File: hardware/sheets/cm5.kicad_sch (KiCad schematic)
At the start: 28 parts, among them J3 microSD, J4 RJ45 GbE magjack UDE RB1-125B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, J40 Fan GND/5V/TACH/PWM, J41 OLED GND/VCC/SCL/SDA, J5 USB-C rpiboot, J6 nRPIBOOT, J7 UART0 GND/TX/RX, M1 CM5002016 (J1), M2 CM5002016 (J2), Q1 2N7002, SW1 DIP x8

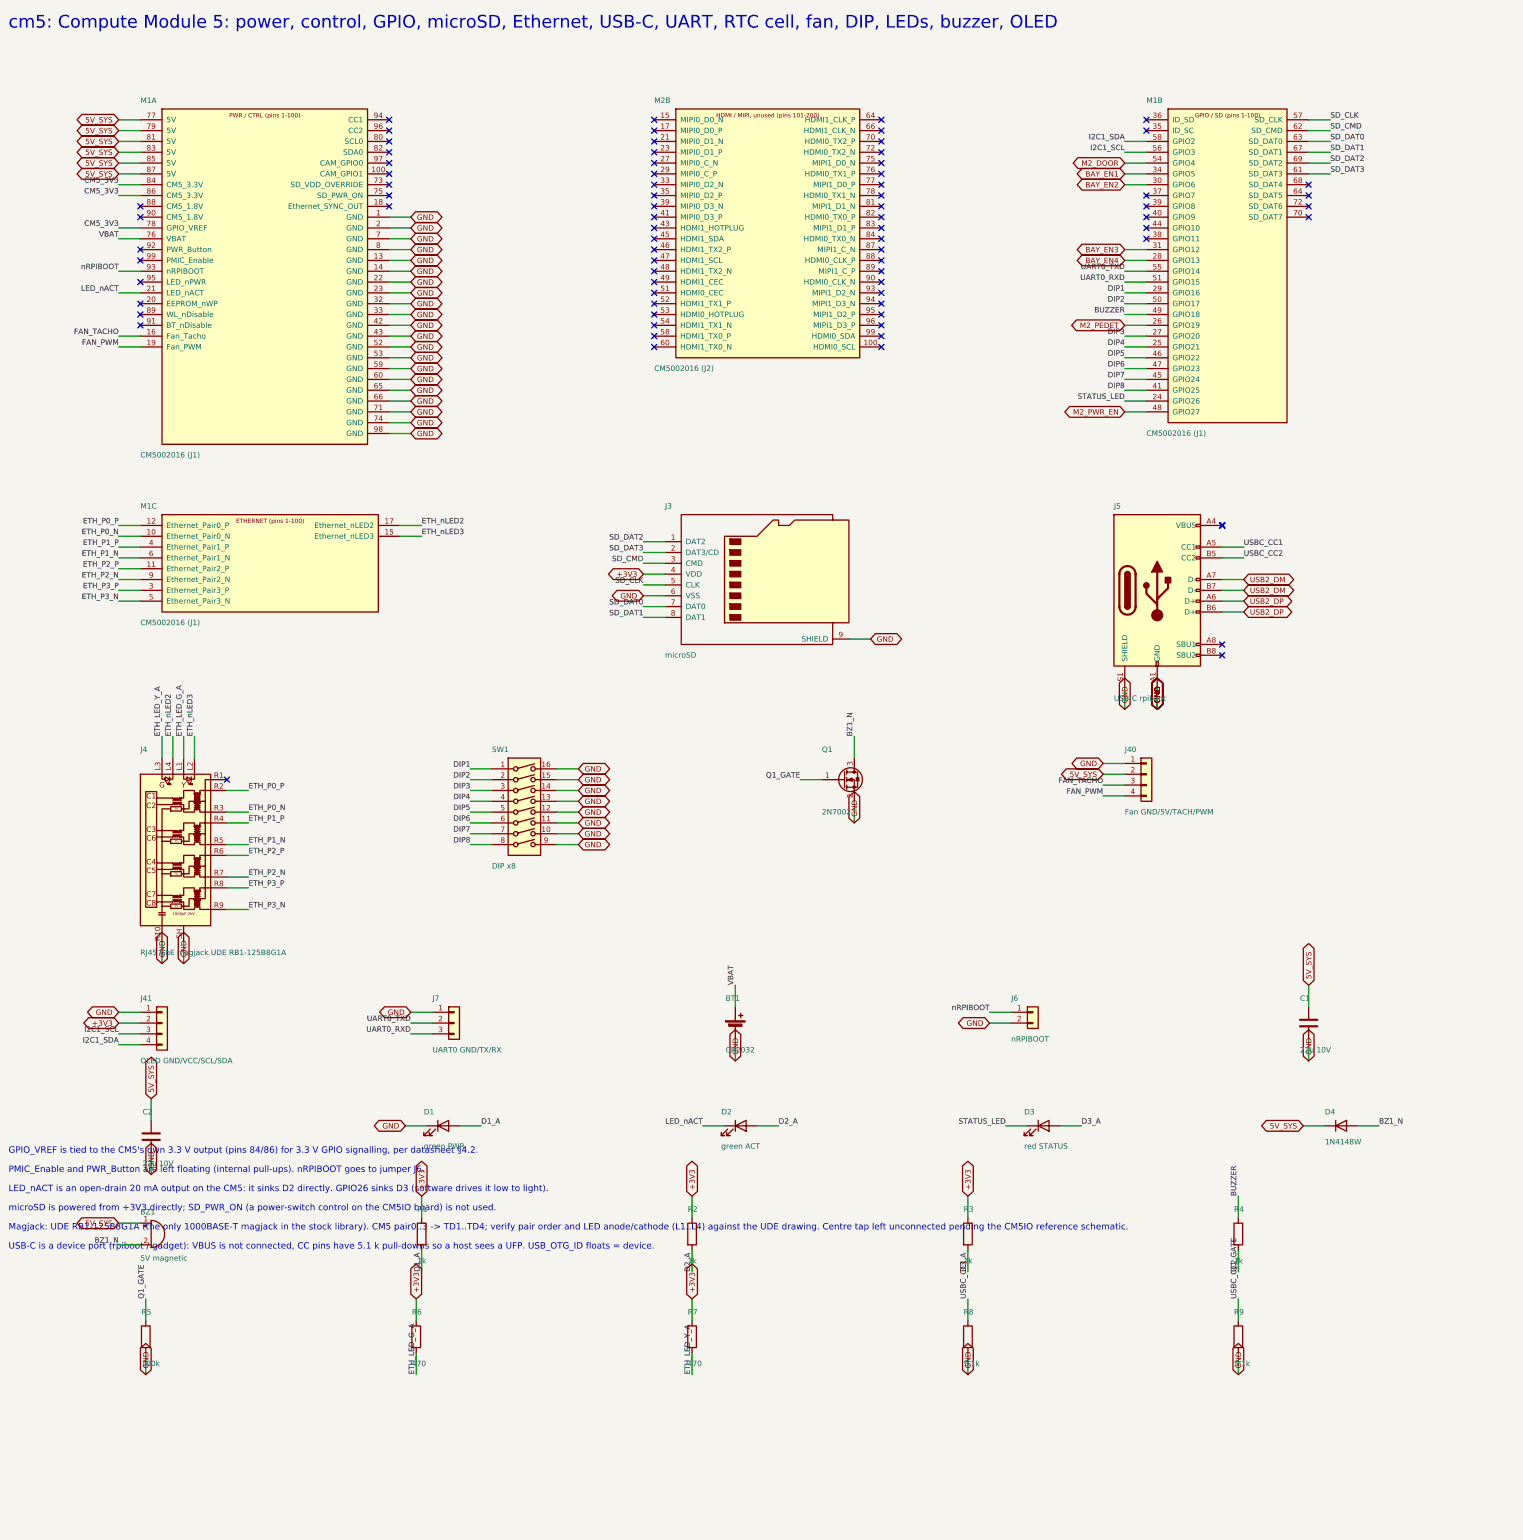
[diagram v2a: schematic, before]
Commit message: hardware: CM5 on the official 204-pad footprint, CM5IO M.2 footprint, reference-design fixes
From the Raspberry Pi CM5IO rev 2 KiCad files: single CM5 footprint with both
connectors and mounting holes; M.2 socket footprint; USB-C CC pins to the CM5;
fan PWM pull-up; microSD through a load switch on SD_PWR_ON; M.2 shield and
standoff pads to GND; PCIe polarity note. Board regenerated with the module
and M.2 at their real sizes; centre mounting hole dropped.

Co-Authored-By: Claude Fable 5.1 <noreply@anthropic.com>
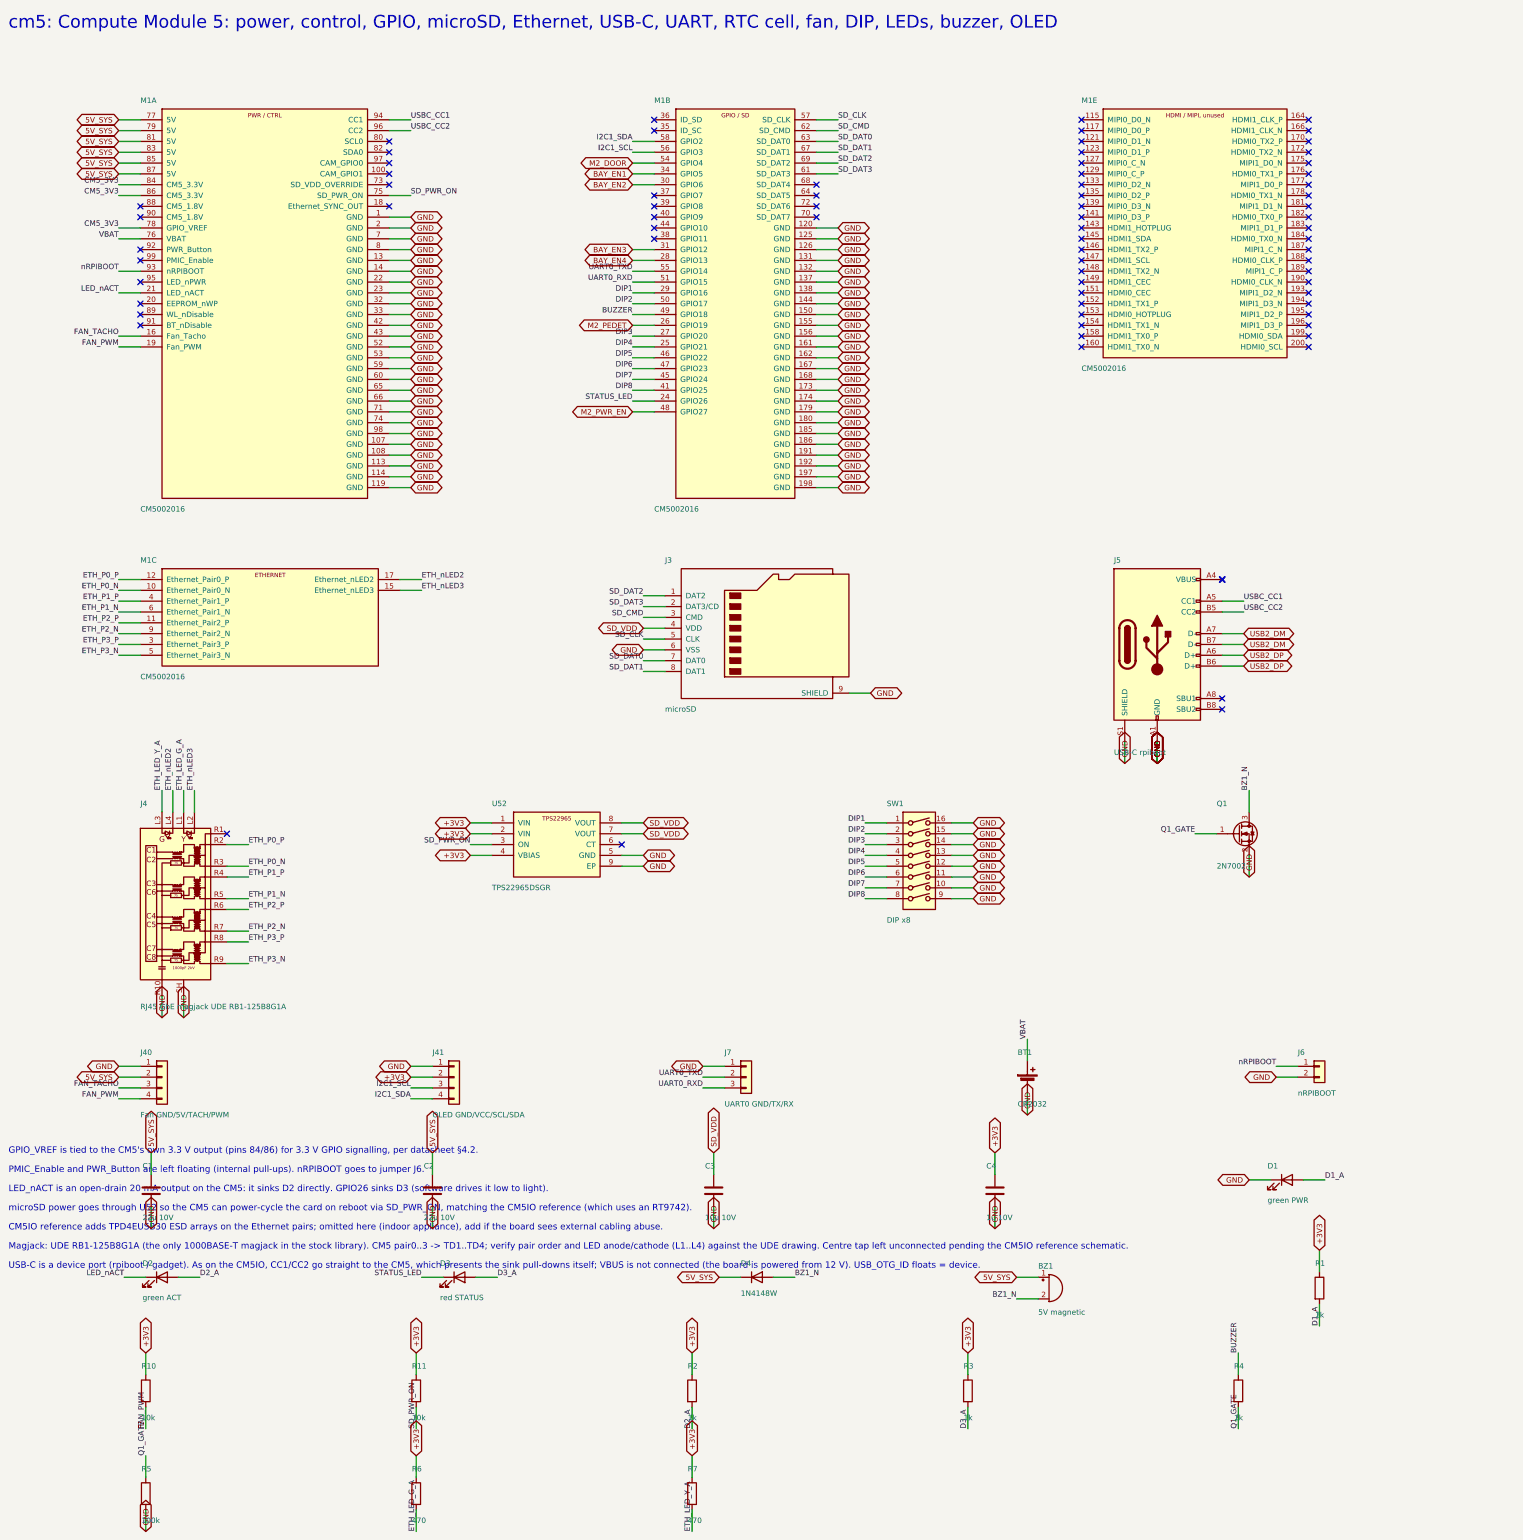
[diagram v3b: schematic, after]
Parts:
- added R5: 100k, Resistor_SMD:R_0402_1005Metric, symbol Device:R
- added R6, R7: 470, Resistor_SMD:R_0402_1005Metric, symbol Device:R
- BT1: renamed from J6; value nRPIBOOT -> CR2032; footprint Connector_PinHeader_2.54mm:PinHeader_1x02_P2.54mm_Vertical -> Battery:BatteryHolder_Keystone_1060_1x2032; symbol Connector_Generic:Conn_01x02 -> Device:Battery_Cell
- BZ1: renamed from R3; value 1k -> 5V magnetic; footprint Resistor_SMD:R_0603_1608Metric -> Buzzer_Beeper:Buzzer_12x9.5RM7.6; symbol Device:R -> Device:Buzzer
- C2: renamed from D1; value green PWR -> 22u 10V; footprint LED_THT:LED_D3.0mm -> Capacitor_SMD:C_0805_2012Metric; symbol Device:LED -> Device:C
- C3: renamed from D2; value green ACT -> 10u 10V; footprint LED_THT:LED_D3.0mm -> Capacitor_SMD:C_0805_2012Metric; symbol Device:LED -> Device:C
- C4: renamed from D3; value red STATUS -> 1u 10V; footprint LED_THT:LED_D3.0mm -> Capacitor_SMD:C_0402_1005Metric; symbol Device:LED -> Device:C
- D1: renamed from D4; value 1N4148W -> green PWR; footprint Diode_SMD:D_SOD-123 -> LED_THT:LED_D3.0mm; symbol Device:D -> Device:LED
- D2: renamed from BZ1; value 5V magnetic -> green ACT; footprint Buzzer_Beeper:Buzzer_12x9.5RM7.6 -> LED_THT:LED_D3.0mm; symbol Device:Buzzer -> Device:LED
- D3: renamed from R1; value 1k -> red STATUS; footprint Resistor_SMD:R_0603_1608Metric -> LED_THT:LED_D3.0mm; symbol Device:R -> Device:LED
- D4: renamed from R2; value 1k -> 1N4148W; footprint Resistor_SMD:R_0603_1608Metric -> Diode_SMD:D_SOD-123; symbol Device:R -> Device:D
- J40: renamed from J41; value OLED GND/VCC/SCL/SDA -> Fan GND/5V/TACH/PWM; footprint Connector_PinHeader_2.54mm:PinHeader_1x04_P2.54mm_Vertical -> Connector:FanPinHeader_1x04_P2.54mm_Vertical
- J41: renamed from J7; value UART0 GND/TX/RX -> OLED GND/VCC/SCL/SDA; footprint Connector_PinHeader_2.54mm:PinHeader_1x03_P2.54mm_Vertical -> Connector_PinHeader_2.54mm:PinHeader_1x04_P2.54mm_Vertical; symbol Connector_Generic:Conn_01x03 -> Connector_Generic:Conn_01x04
- J6: renamed from C1; value 22u 10V -> nRPIBOOT; footprint Capacitor_SMD:C_0805_2012Metric -> Connector_PinHeader_2.54mm:PinHeader_1x02_P2.54mm_Vertical; symbol Device:C -> Connector_Generic:Conn_01x02
- J7: renamed from BT1; value CR2032 -> UART0 GND/TX/RX; footprint Battery:BatteryHolder_Keystone_1060_1x2032 -> Connector_PinHeader_2.54mm:PinHeader_1x03_P2.54mm_Vertical; symbol Device:Battery_Cell -> Connector_Generic:Conn_01x03
- M1: value CM5002016 (J1) -> CM5002016; footprint Connector_Hirose_DF40:Hirose_DF40C-100DS-0.4V_2x50_P0.4mm -> brain-drain:Raspberry-Pi-5-Compute-Module; symbol brain-drain:CM5_J1 -> brain-drain:CM5
- M1: renamed from M2; value CM5002016 (J2) -> CM5002016; footprint Connector_Hirose_DF40:Hirose_DF40C-100DS-0.4V_2x50_P0.4mm -> brain-drain:Raspberry-Pi-5-Compute-Module; symbol brain-drain:CM5_J2 -> brain-drain:CM5
- Q1: renamed from J40; value Fan GND/5V/TACH/PWM -> 2N7002; footprint Connector:FanPinHeader_1x04_P2.54mm_Vertical -> Package_TO_SOT_SMD:SOT-23; symbol Connector_Generic:Conn_01x04 -> Transistor_FET:2N7002
- R1: renamed from R4; footprint Resistor_SMD:R_0402_1005Metric -> Resistor_SMD:R_0603_1608Metric
- R10: renamed from R5; value 100k -> 10k
- R11: renamed from R6; value 470 -> 10k
- R2: renamed from R7; value 470 -> 1k; footprint Resistor_SMD:R_0402_1005Metric -> Resistor_SMD:R_0603_1608Metric
- R3: renamed from R8; value 5.1k -> 1k; footprint Resistor_SMD:R_0402_1005Metric -> Resistor_SMD:R_0603_1608Metric
- R4: renamed from R9; value 5.1k -> 1k
- SW1: renamed from Q1; value 2N7002 -> DIP x8; footprint Package_TO_SOT_SMD:SOT-23 -> Button_Switch_THT:SW_DIP_SPSTx08_Piano_10.8x21.88mm_W7.62mm_P2.54mm; symbol Transistor_FET:2N7002 -> Switch:SW_DIP_x08
- U52: renamed from SW1; value DIP x8 -> TPS22965DSGR; footprint Button_Switch_THT:SW_DIP_SPSTx08_Piano_10.8x21.88mm_W7.62mm_P2.54mm -> Package_SON:Texas_DSG0008A_WSON-8-1EP_2x2mm_P0.5mm_EP0.9x1.6mm; symbol Switch:SW_DIP_x08 -> brain-drain:TPS22965
- renumbered C2 to C1
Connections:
- net +3V3: now also C4.1, J41.2 (Pin_2), R1.1, R10.1, R3.1, U52.1 (VIN), U52.2 (VIN), U52.4 (VBIAS), R6.1, R7.1; no longer BZ1.1, D3.1, D4.1, J3.4 (VDD), J40.2 (Pin_2)
- net 5V_SYS: now also BZ1.1 (+), C2.1, D4.1 (K), J40.2 (Pin_2); no longer D1.1 (K), D2.1 (+), J6.1, Q1.2 (Pin_2)
- net BAY_EN1: now also M1.34 (GPIO5); no longer M1.34 (GPIO5)
- net BAY_EN2: now also M1.30 (GPIO6); no longer M1.30 (GPIO6)
- net BAY_EN3: now also M1.31 (GPIO12); no longer M1.31 (GPIO12)
- net BAY_EN4: now also M1.28 (GPIO13); no longer M1.28 (GPIO13)
- net BUZZER: now also M1.49 (GPIO18), R4.1; no longer M1.49 (GPIO18), R1.1
- net BZ1_N: now also BZ1.2 (-), D4.2 (A), Q1.3 (D); no longer D1.2 (A), D2.2 (-), SW1.3 (D)
- net D1_A: now also D1.2 (A), R1.2; no longer C2.2 (A), D3.2
- net D2_A: now also D2.2 (A), R2.2; no longer C3.2 (A), D4.2
- net D3_A: now also D3.2 (A), R3.2; no longer BZ1.2, C4.2 (A)
- net DIP1: now also M1.29 (GPIO16), SW1.1; no longer M1.29 (GPIO16), U52.1
- net DIP2: now also M1.50 (GPIO17), SW1.2; no longer M1.50 (GPIO17), U52.2
- net DIP3: now also M1.27 (GPIO20), SW1.3; no longer M1.27 (GPIO20), U52.3
- net DIP4: now also M1.25 (GPIO21), SW1.4; no longer M1.25 (GPIO21), U52.4
- net DIP5: now also M1.46 (GPIO22), SW1.5; no longer M1.46 (GPIO22), U52.5
- net DIP6: now also M1.47 (GPIO23), SW1.6; no longer M1.47 (GPIO23), U52.6
- net DIP7: now also M1.45 (GPIO24), SW1.7; no longer M1.45 (GPIO24), U52.7
- net DIP8: now also M1.41 (GPIO25), SW1.8; no longer M1.41 (GPIO25), U52.8
- net ETH_LED_G_A: now also R6.2; no longer R11.2
- net ETH_LED_Y_A: now also R7.2; no longer R2.2
- net FAN_PWM: now also J40.4 (Pin_4), R10.2; no longer Q1.4 (Pin_4)
- net FAN_TACHO: now also J40.3 (Pin_3); no longer Q1.3 (Pin_3)
- net GND: now also C2.2, C3.2, C4.2, D1.1 (K), J7.1 (Pin_1), M1.107 (GND), M1.108 (GND), M1.113 (GND), M1.114 (GND), M1.119 (GND), M1.120 (GND), M1.125 (GND), M1.126 (GND), M1.131 (GND), M1.132 (GND), M1.137 (GND), M1.138 (GND), M1.144 (GND), M1.150 (GND), M1.155 (GND), M1.156 (GND), M1.161 (GND), M1.162 (GND), M1.167 (GND), M1.168 (GND), M1.173 (GND), M1.174 (GND), M1.179 (GND), M1.180 (GND), M1.185 (GND), M1.186 (GND), M1.191 (GND), M1.192 (GND), M1.197 (GND), M1.198 (GND), Q1.2 (S), SW1.10, SW1.11, SW1.12, SW1.13, SW1.14, SW1.15, SW1.16, SW1.9, U52.5 (GND), R5.2; no longer C2.1 (K), J7.2 (-), Q1.1 (Pin_1), R10.2, R3.2, R4.2, SW1.2 (S), U52.10, U52.11, U52.12, U52.13, U52.14, U52.15, U52.16
- net I2C1_SCL: now also J41.3 (Pin_3), M1.56 (GPIO3); no longer J40.3 (Pin_3), M1.56 (GPIO3)
- net I2C1_SDA: now also J41.4 (Pin_4), M1.58 (GPIO2); no longer J40.4 (Pin_4), M1.58 (GPIO2)
- net LED_nACT: now also D2.1 (K); no longer C3.1 (K)
- net M2_DOOR: now also M1.54 (GPIO4); no longer M1.54 (GPIO4)
- net M2_PEDET: now also M1.26 (GPIO19); no longer M1.26 (GPIO19)
- net M2_PWR_EN: now also M1.48 (GPIO27); no longer M1.48 (GPIO27)
- net Q1_GATE: now also Q1.1 (G), R4.2, R5.1; no longer R1.2, R10.1, SW1.1 (G)
- net SD_CLK: now also M1.57 (SD_CLK); no longer M1.57 (SD_CLK)
- net SD_CMD: now also M1.62 (SD_CMD); no longer M1.62 (SD_CMD)
- net SD_DAT0: now also M1.63 (SD_DAT0); no longer M1.63 (SD_DAT0)
- net SD_DAT1: now also M1.67 (SD_DAT1); no longer M1.67 (SD_DAT1)
- net SD_DAT2: now also M1.69 (SD_DAT2); no longer M1.69 (SD_DAT2)
- net SD_DAT3: now also M1.61 (SD_DAT3); no longer M1.61 (SD_DAT3)
- net STATUS_LED: now also D3.1 (K), M1.24 (GPIO26); no longer C4.1 (K), M1.24 (GPIO26)
- net UART0_RXD: now also J7.3 (Pin_3), M1.51 (GPIO15); no longer J41.3 (Pin_3), M1.51 (GPIO15)
- net UART0_TXD: now also J7.2 (Pin_2), M1.55 (GPIO14); no longer J41.2 (Pin_2), M1.55 (GPIO14)
- net USBC_CC1: now also M1.94 (CC1); no longer R3.1
- net USBC_CC2: now also M1.96 (CC2); no longer R4.1
- net VBAT: now also BT1.1 (+); no longer J7.1 (+)
- net nRPIBOOT: now also J6.1 (Pin_1); no longer BT1.1 (Pin_1)
- net SD_PWR_ON: now reaches M1.75 (SD_PWR_ON)
- net SD_PWR_ON: now also R11.2, U52.3 (ON)
- new net SD_VDD: C3.1, J3.4 (VDD), U52.7 (VOUT), U52.8 (VOUT)
- no-connect marks 79 -> 77
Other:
- note added: "CM5IO reference adds TPD4EUSB30 ESD arrays on the Ethernet pairs; omitted here (indoor appliance), add if the board sees external cabling abuse."
- note added: "USB-C is a device port (rpiboot / gadget). As on the CM5IO, CC1/CC2 go straight to the CM5, which presents the sink pull-downs itself; VBUS is not connected (the board is powered from 12 V). USB_OTG_ID floats = device."
- note added: "microSD power goes through U52 so the CM5 can power-cycle the card on reboot via SD_PWR_ON, matching the CM5IO reference (which uses an RT9742)."
- note removed: "USB-C is a device port (rpiboot / gadget): VBUS is not connected, CC pins have 5.1 k pull-downs so a host sees a UFP. USB_OTG_ID floats = device."
- note removed: "microSD is powered from +3V3 directly; SD_PWR_ON (a power-switch control on the CM5IO board) is not used."
- moved on the sheet: C1, J3, J4, J40, J5, M1C, R1, R10, R11, R2, R3, R4
